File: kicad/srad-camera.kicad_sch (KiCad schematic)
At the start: 11 parts, among them J1 SWD

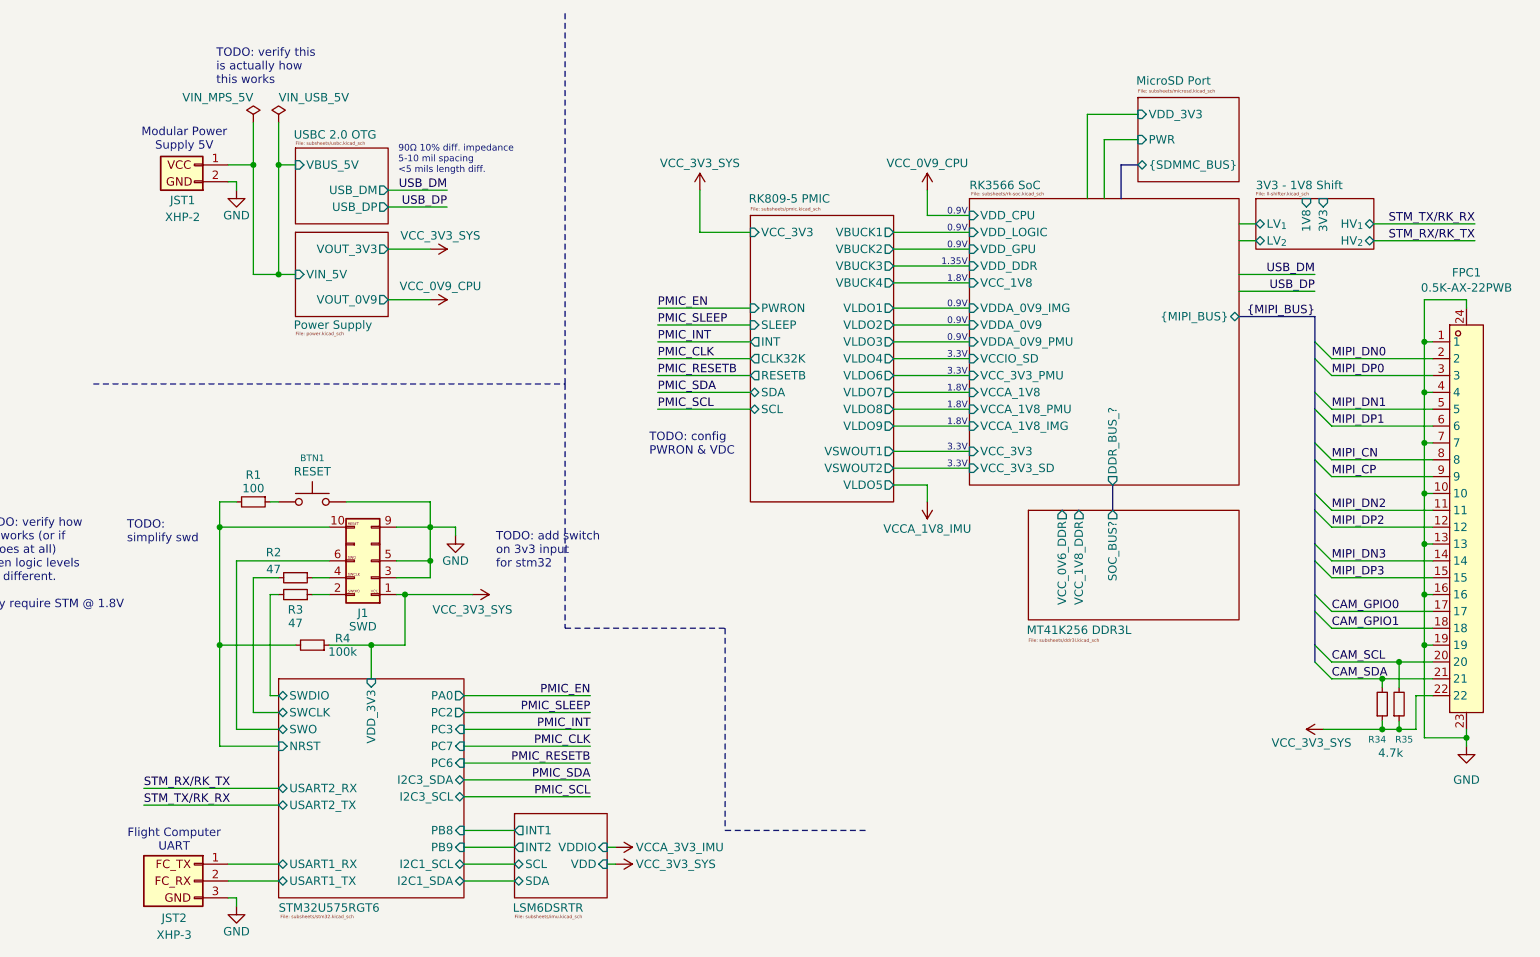
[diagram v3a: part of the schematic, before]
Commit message: Remove uneeded level shifter
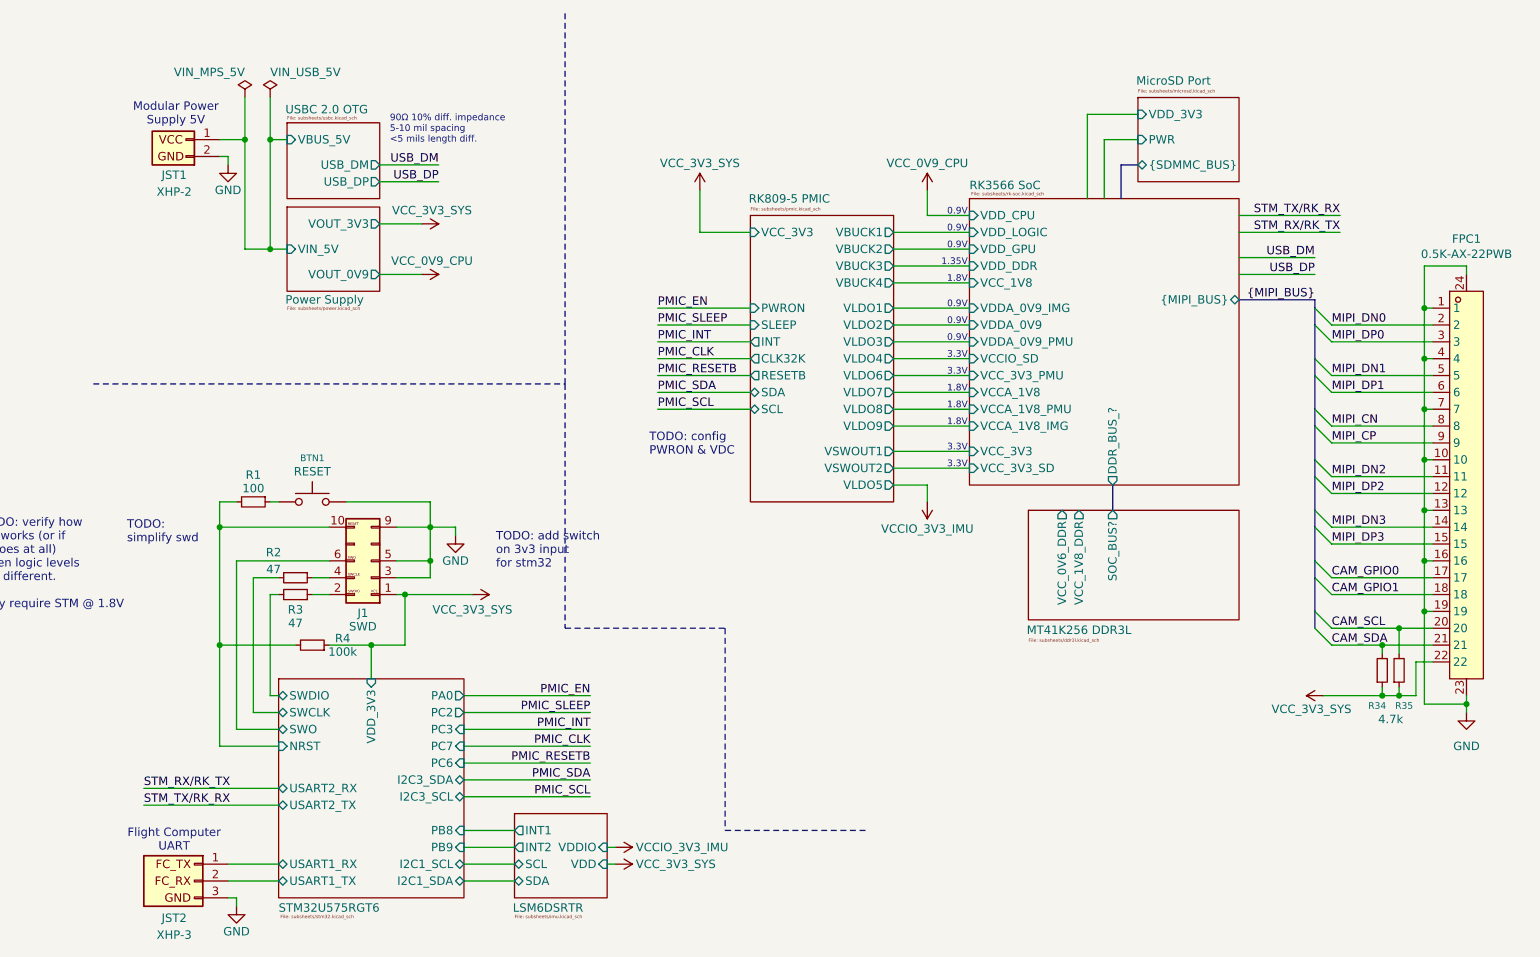
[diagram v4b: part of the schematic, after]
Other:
- removed sheet 3V3 - 1V8 Shift
- sheet Power Supply: file power.kicad_sch -> subsheets/power.kicad_sch
- note removed: "TODO: verify this is actually how this works"
- moved on the sheet: FPC1, JST1, R34, R35

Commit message: Clean up debug connector, STM pinout
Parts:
- removed BTN1: RESET, symbol Switch:SW_Push
- removed R1: 100, symbol Device:R_Small
- removed R2, R3: 47, symbol Device:R_Small
- removed R4: 100k, symbol Device:R_Small
- added R39: 100k, symbol Device:R_Small
- added R6, R8: 47, symbol Device:R_Small
- J1: value SWD -> DEBUG
- JST1: value XHP-2 -> XHP-3; symbol Connector_Generic:Conn_01x02 -> Connector_Generic:Conn_01x03
- JST2: value XHP-3 -> XHP-2; symbol Connector_Generic:Conn_01x03 -> Connector_Generic:Conn_01x02
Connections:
- net GND: now also JST1.3 (Pin_3); no longer JST1.2 (Pin_2), JST2.3 (Pin_3)
- net STM32U575RGT6/NRST: now also R39.2
- net STM32U575RGT6/SWCLK: now also R8.1
- net STM32U575RGT6/SWDIO: now also R6.1
- net STM32U575RGT6/USART1_RX: now also JST2.2 (Pin_2); no longer JST2.1 (Pin_1)
- net STM32U575RGT6/USART1_TX: now also JST2.1 (Pin_1); no longer JST2.2 (Pin_2)
- net VCC_3V3_SYS: now also R39.1
- net at J1.4 (Pin_4): now also R8.2
- net at J1.2 (Pin_2): now also R6.2
- no-connect marks 0 -> 1
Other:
- sheet MT41K256 DDR3L ports: added WIP; removed SOC_BUS?
- sheet MicroSD Port ports: added SDMMC_PWR; removed PWR
- sheet RK3566 SoC ports: added WIP; removed DDR_BUS_?
- sheet RK809-5 PMIC ports: added ENABLE; removed PWRON
- sheet STM32U575RGT6 ports: added PC4, PC5; removed PA0, PC7
- note added: "02x22 FPCr 0.5mm pitchr 2-sided contacts"
- note added: "?"
- note added: "Modular Power Supply"
- note added: "RK3566 UART must be configured to match (default: 1.8V)"
- note removed: "Modular Power Supply 5V"
- note removed: "TODO: verify how I/O works (or if it does at all) when logic levels are different. may require STM @ 1.8V"
- moved on the sheet: FPC1, R34, R35

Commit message: Reconfigure STM32 pinout to work better with physical pin locations
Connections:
- net STM32U575RGT6/USART1_RX renamed STM32U575RGT6/USART2_RX
- net STM32U575RGT6/USART1_TX renamed STM32U575RGT6/USART2_TX
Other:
- sheet STM32U575RGT6 ports: added I2C2_SCL, I2C2_SDA, PB12, PB13, PC15, PH0, PH1; removed I2C1_SCL, I2C1_SDA, PB8, PB9, PC4, PC5, PC6
- note added: "TODO: add switch on 3v3 input for stm32 add boot0 add reset"
- note removed: "TODO: add switch on 3v3 input for stm32"
- note removed: "TODO: simplify swd"
- moved on the sheet: JST2, R6, R8
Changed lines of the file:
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@@
 		)
 	)
-	(text "TODO: \nsimplify swd "
-		(exclude_from_sim no)
-		(at -155.194 97.028 0)
-		(effects
-			(font
-				(size 1.27 1.27)
-			)
-			(justify left)
-		)
-	)
 	(text "0.9V"
 		(exclude_from_sim no)
@@
 		)
 	)
-	(text "TODO: add switch\non 3v3 input \nfor stm32"
+	(text "TODO: add switch\non 3v3 input \nfor stm32\n\nadd boot0\nadd reset"
 		(exclude_from_sim no)
-		(at 59.944 77.978 0)
+		(at 44.45 112.014 0)
 		(effects
 			(font
@@
 	(wire
 		(pts
-			(xy 45.72 127) (xy 48.26 127)
+			(xy 44.45 127) (xy 48.26 127)
 		)
 		(stroke
@@
 	(wire
 		(pts
-			(xy 45.72 129.54) (xy 48.26 129.54)
+			(xy 44.45 129.54) (xy 48.26 129.54)
 		)
 		(stroke
@@
 	(wire
 		(pts
-			(xy 36.83 127) (xy 40.64 127)
+			(xy 36.83 127) (xy 39.37 127)
 		)
 		(stroke
@@
 	(wire
 		(pts
-			(xy 36.83 129.54) (xy 40.64 129.54)
+			(xy 36.83 129.54) (xy 39.37 129.54)
 		)
 		(stroke
@@
 	(symbol
 		(lib_id "Device:R_Small")
-		(at 43.18 129.54 270)
+		(at 41.91 129.54 270)
 		(mirror x)
 		(unit 1)
@@
 		(dnp no)
 		(property "Reference" "R8"
-			(at 43.18 131.318 90)
+			(at 41.91 131.318 90)
 			(effects
 				(font
@@
 		)
 		(property "Value" "47"
-			(at 43.18 133.35 90)
+			(at 41.91 133.35 90)
 			(effects
 				(font
@@
 		)
 		(property "Footprint" ""
-			(at 43.18 129.54 0)
+			(at 41.91 129.54 0)
 			(effects
 				(font
@@
 		)
 		(property "Datasheet" "~"
-			(at 43.18 129.54 0)
+			(at 41.91 129.54 0)
 			(effects
 				(font
@@
 		)
 		(property "Description" "Resistor, small symbol"
-			(at 43.18 129.54 0)
+			(at 41.91 129.54 0)
 			(effects
 				(font
@@
 	(symbol
 		(lib_id "Device:R_Small")
-		(at 43.18 127 270)
+		(at 41.91 127 270)
 		(unit 1)
 		(exclude_from_sim no)
@@
 		(dnp no)
 		(property "Reference" "R6"
-			(at 46.228 125.984 90)
+			(at 45.466 125.984 90)
 			(effects
 				(font
@@
 		)
 		(property "Value" "47"
-			(at 46.228 128.016 90)
+			(at 45.466 128.016 90)
 			(effects
 				(font
@@
 		)
 		(property "Footprint" ""
-			(at 43.18 127 0)
+			(at 41.91 127 0)
 			(effects
 				(font
@@
 		)
 		(property "Datasheet" "~"
-			(at 43.18 127 0)
+			(at 41.91 127 0)
 			(effects
 				(font
@@
 		)
 		(property "Description" "Resistor, small symbol"
-			(at 43.18 127 0)
+			(at 41.91 127 0)
 			(effects
 				(font
@@
 		(lib_name "Conn_01x02_1")
 		(lib_id "Connector_Generic:Conn_01x02")
-		(at 34.29 153.67 0)
-		(mirror y)
+		(at 34.29 153.67 180)
 		(unit 1)
 		(exclude_from_sim no)
@@
 		)
 		(property "Datasheet" "~"
-			(at 35.56 152.4 0)
+			(at 35.56 154.94 0)
 			(effects
 				(font
@@
 		)
 		(property "Description" "Generic connector, single row, 01x02, script generated (kicad-library-utils/schlib/autogen/connector/)"
-			(at 35.56 152.4 0)
+			(at 35.56 154.94 0)
 			(effects
 				(font
@@
 			)
 		)
-		(pin "I2C1_SCL" bidirectional
-			(at 76.2 152.4 0)
+		(pin "PC2" output
+			(at 76.2 127 0)
 			(effects
 				(font
@@
 			)
 		)
-		(pin "I2C1_SDA" bidirectional
-			(at 76.2 154.94 0)
+		(pin "PC3" output
+			(at 76.2 129.54 0)
 			(effects
 				(font
@@
 			)
 		)
-		(pin "I2C3_SCL" bidirectional
-			(at 76.2 142.24 0)
+		(pin "I2C2_SCL" bidirectional
+			(at 76.2 152.4 0)
 			(effects
 				(font
@@
 			)
 		)
-		(pin "I2C3_SDA" bidirectional
-			(at 76.2 139.7 0)
+		(pin "I2C2_SDA" bidirectional
+			(at 76.2 154.94 0)
 			(effects
 				(font
@@
 			)
 		)
-		(pin "PB8" input
-			(at 76.2 147.32 0)
+		(pin "I2C3_SCL" bidirectional
+			(at 76.2 142.24 0)
 			(effects
 				(font
@@
 			)
 		)
-		(pin "PB9" input
-			(at 76.2 149.86 0)
+		(pin "I2C3_SDA" bidirectional
+			(at 76.2 139.7 0)
 			(effects
 				(font
@@
 			)
 		)
-		(pin "USART1_TX" bidirectional
-			(at 48.26 152.4 180)
+		(pin "PB12" input
+			(at 76.2 147.32 0)
 			(effects
 				(font
 					(size 1.27 1.27)
 				)
-				(justify left)
+				(justify right)
 			)
 		)
-		(pin "USART1_RX" bidirectional
-			(at 48.26 154.94 180)
+		(pin "PB13" input
+			(at 76.2 149.86 0)
 			(effects
 				(font
 					(size 1.27 1.27)
 				)
-				(justify left)
+				(justify right)
 			)
 		)
-		(pin "USART2_RX" bidirectional
-			(at 48.26 140.97 180)
+		(pin "PC15" input
+			(at 76.2 132.08 0)
 			(effects
 				(font
 					(size 1.27 1.27)
 				)
-				(justify left)
+				(justify right)
 			)
 		)
-		(pin "USART2_TX" bidirectional
-			(at 48.26 143.51 180)
+		(pin "PH0" input
+			(at 76.2 134.62 0)
 			(effects
 				(font
 					(size 1.27 1.27)
 				)
-				(justify left)
+				(justify right)
 			)
 		)
-		(pin "PC2" output
-			(at 76.2 127 0)
+		(pin "PH1" input
+			(at 76.2 137.16 0)
 			(effects
 				(font
@@
 			)
 		)
-		(pin "PC3" output
-			(at 76.2 129.54 0)
+		(pin "USART1_RX" bidirectional
+			(at 48.26 140.97 180)
 			(effects
 				(font
 					(size 1.27 1.27)
 				)
-				(justify right)
+				(justify left)
 			)
 		)
-		(pin "PC4" input
-			(at 76.2 132.08 0)
+		(pin "USART1_TX" bidirectional
+			(at 48.26 143.51 180)
 			(effects
 				(font
 					(size 1.27 1.27)
 				)
-				(justify right)
+				(justify left)
 			)
 		)
-		(pin "PC5" input
-			(at 76.2 134.62 0)
+		(pin "USART2_RX" bidirectional
+			(at 48.26 152.4 180)
 			(effects
 				(font
 					(size 1.27 1.27)
 				)
-				(justify right)
+				(justify left)
 			)
 		)
-		(pin "PC6" input
-			(at 76.2 137.16 0)
+		(pin "USART2_TX" bidirectional
+			(at 48.26 154.94 180)
 			(effects
 				(font
 					(size 1.27 1.27)
 				)
-				(justify right)
+				(justify left)
 			)
 		)

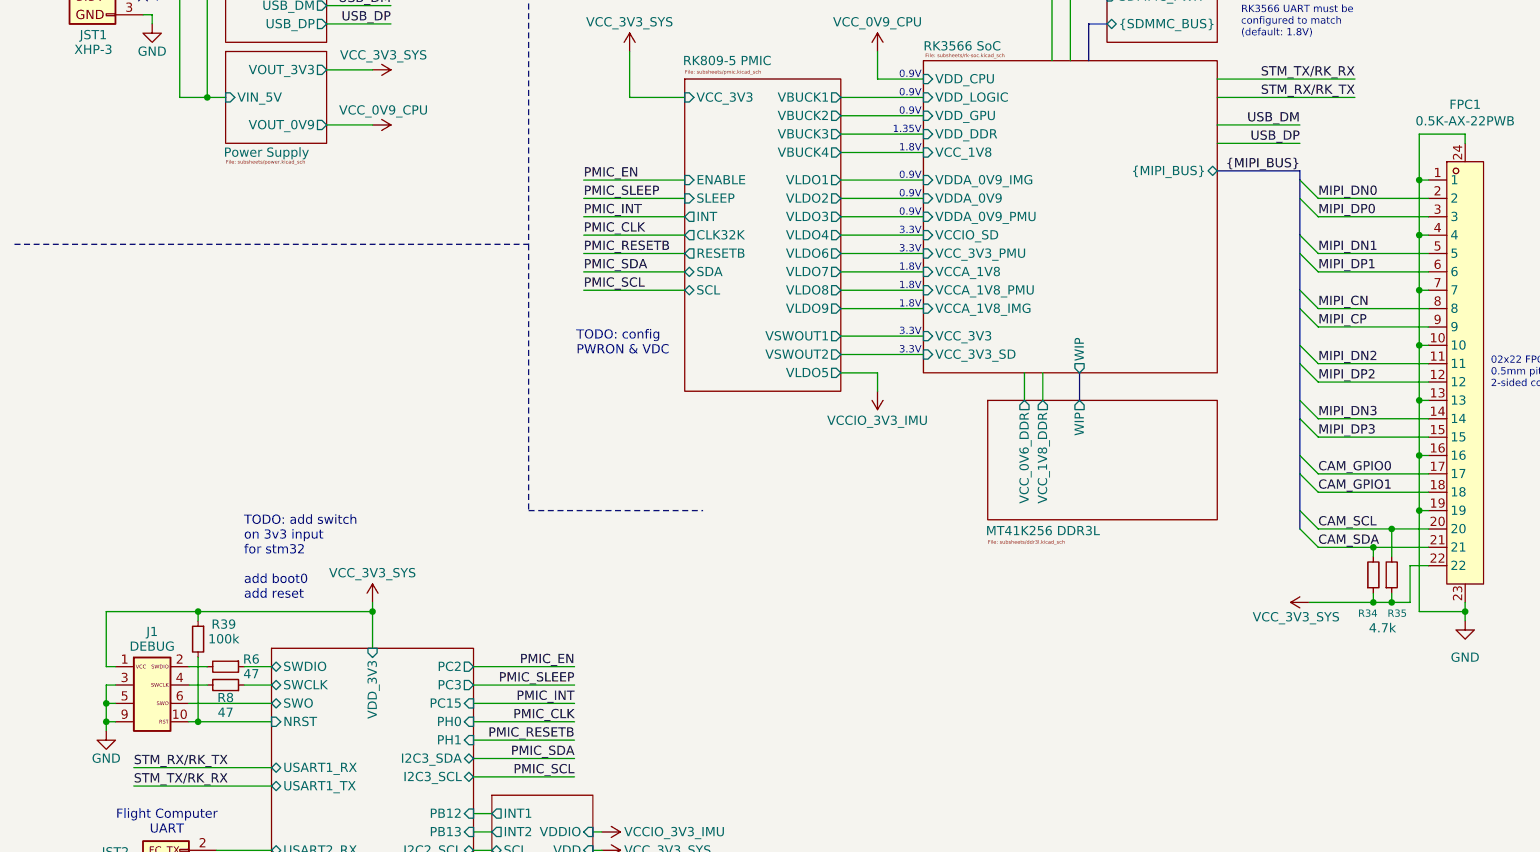
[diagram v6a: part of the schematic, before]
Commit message: Added boot + power switch to STM32, user button
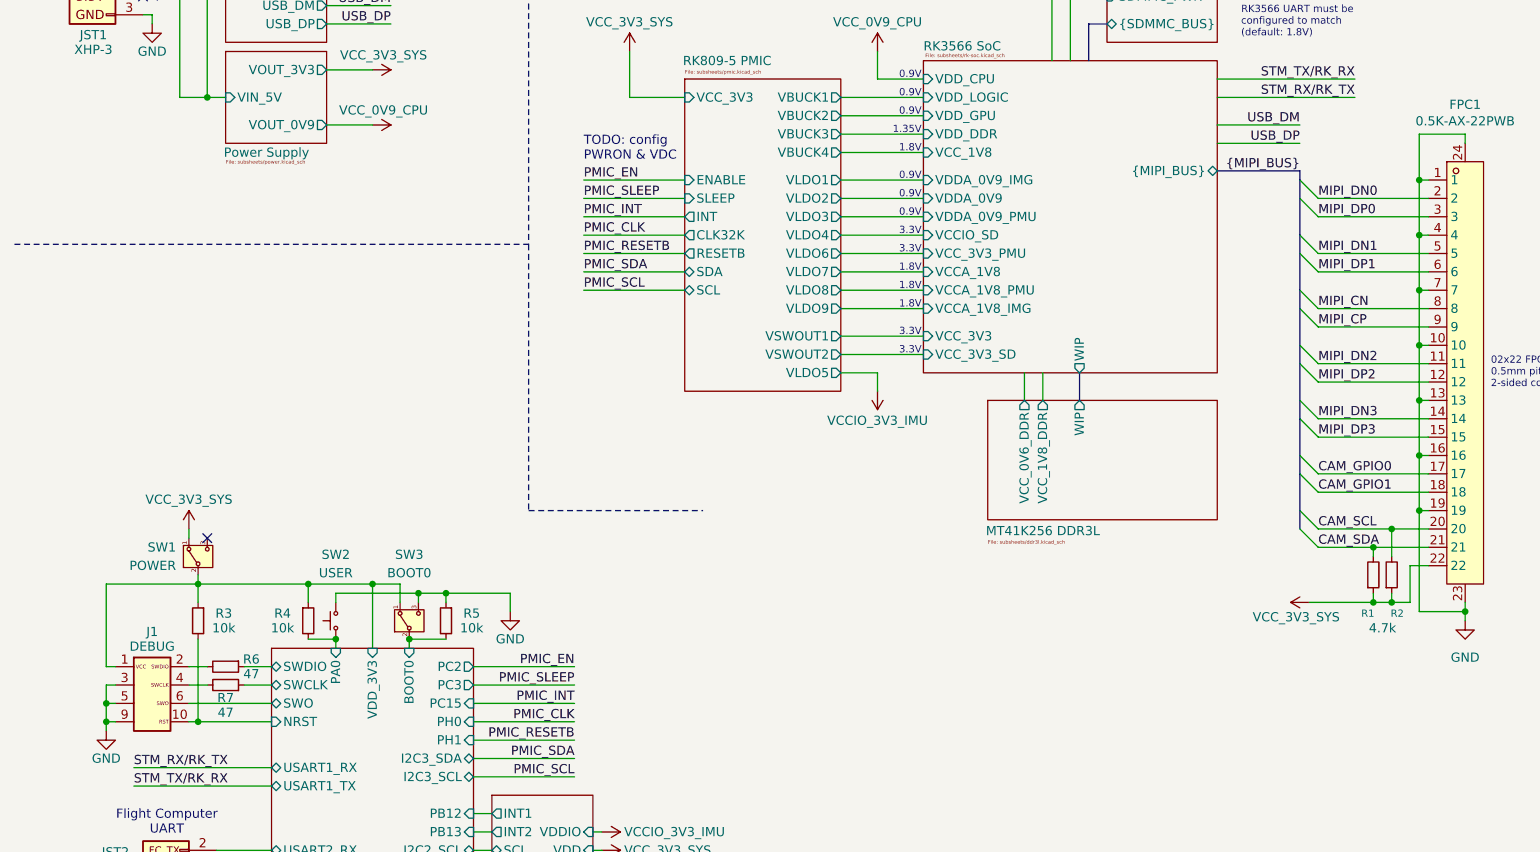
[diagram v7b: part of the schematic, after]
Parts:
- added R4, R5: 10k, symbol Device:R_Small
- added SW1: POWER, symbol Switch:SW_SPDT
- added SW2: USER, symbol Switch:SW_Push
- added SW3: BOOT0, symbol Switch:SW_SPDT
- R3: renamed from R39; value 100k -> 10k
- renumbered R34 to R1, R35 to R2, R8 to R7
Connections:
- net GND: now also R5.1, SW2.2, SW3.3 (C)
- net VCC_3V3_SYS: now also SW1.1 (A); no longer J1.1 (Pin_1), R3.1
- new net STM32U575RGT6/BOOT0: R5.2, SW3.2 (B)
- new net STM32U575RGT6/PA0: R4.2, SW2.1
- new net STM32U575RGT6/VDD_3V3: J1.1 (Pin_1), R3.1, R4.1, SW1.2 (B), SW3.1 (A)
- no-connect marks 1 -> 2
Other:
- sheet STM32U575RGT6 ports: added BOOT0, PA0; removed none
- note removed: "TODO: add switch on 3v3 input for stm32 add boot0 add reset"
- moved on the sheet: R3
